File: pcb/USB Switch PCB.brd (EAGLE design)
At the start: 36 parts, among them Q1 2N7002P, Q2 2N7002P, Q3 12 MHz, X1 AMPHENOL-0001LF, X2 UE27-USBA, X3 AMPHENOL-0001LF

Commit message: Starting to look good.
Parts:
- added R10, R11: 100Ω, rcl:R0603
- added R7, R8, R9: 12kΩ, rcl:R0603
- moved EXTPWR 99.8 mm to (22.3, 2.23)
- moved R5 97.0 mm to (57.7, 9.30), turned to 0 degrees
- moved S1 96.9 mm to (26.6, 11.4)
- moved R6 96.2 mm to (57.7, 11.3), turned to 180 degrees
- moved U$4 95.8 mm to (53.9, 16.2)
- moved C9 89.6 mm to (57.7, 13.4), turned to 180 degrees
- moved C3 88.0 mm to (52.8, 12.9), turned to 270 degrees
- moved UIN 86.6 mm to (11.0, 6.97)
- moved LED2 86.3 mm to (4.93, 3.29)
- moved R2 86.3 mm to (4.93, 3.46)
- moved C4 86.3 mm to (50.7, 12.9), turned to 270 degrees
- moved X1 86.2 mm to (11.0, 1.14)
- moved R3 85.9 mm to (38.6, 13.8), turned to 90 degrees
- moved U$5 85.7 mm to (37.0, 8.66)
- moved R1 85.6 mm to (17.1, 3.33)
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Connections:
- new net GPIO15: MCU.10, R9.2
- new net GPIO2: MCU.11, R8.2
- new net N$3: MCU.14, R10.1
- new net N$5: MCU.13, R11.1
- net +5V: now also R7.1, R8.1
- net DATAGATE: now also R11.2; no longer MCU.14
- net GND: now also R9.1
- net GPIO0: now also R7.2
- net POWERGATE: now also R10.2; no longer MCU.13
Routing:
- net +5V: track 0.00 -> 127.7 mm, vias 0 -> 1
- net VCCI: track 0.00 -> 48.2 mm
- net DATAGATE: track 0.00 -> 38.9 mm
- net DATACOIL: track 0.00 -> 37.8 mm
- net +3V3: track 0.00 -> 30.0 mm, vias 0 -> 2
- net RST: track 0.00 -> 27.3 mm, vias 0 -> 1
- net GNDO: track 0.00 -> 23.3 mm
- net TXD: track 0.00 -> 21.9 mm, vias 0 -> 1
- net RXD: track 0.00 -> 17.6 mm, vias 0 -> 1
- net VCCO: track 0.00 -> 17.5 mm
- net POWERCOIL: track 0.00 -> 17.4 mm
- net POWERGATE: track 0.00 -> 15.7 mm
- net GPIO0: track 0.00 -> 13.7 mm, vias 0 -> 2
- net D-ESP: track 0.00 -> 13.5 mm
- net D+I: track 0.00 -> 13.5 mm
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- added copper zone on layer 1, net GND
- added copper zone on layer 16, net GND
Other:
- board outline added: 62.8 x 30 mm
- board text added: "EXTPWR + -"
- board text added: "USB Switch 1.1 git.erim.se/hw/usb-switch"
- board text removed: "EXT + -"
- board text removed: "USB Switch 1.1 git.erim.se /hw/usb-switch"

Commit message: Converting everything
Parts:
- removed C3: 10µF, rcl:C0603
- removed C4: 100nF, rcl:C0603
- removed D3: BAS21LT1, USB Switch PCB:SOT23
- removed R5, R6: 470Ω, rcl:R0603
- removed U$3: CH340G, ch340g:SOIC16
- removed U$4: UMH3N, USB Switch PCB:SOT363
- removed UIN: (no value), USB Switch PCB:FE05-1
- removed UOUT: (no value), USB Switch PCB:FE04-1
- removed X1, X3: AMPHENOL-0001LF, USB Switch PCB:10118192-0001LF
- added FLASH, RESET: MOMENTARY-SWITCH, USB Switch PCB:MOMENTARY-SWITCH
- added J1: (no value), SparkFun-Connectors:1X06
- added U$6: USB-B, USB Switch PCB:USB-B
- moved LED2 4.58 mm to (2.39, 7.11)
- moved R2 4.58 mm to (2.39, 7.26)
- moved LED1 4.02 mm to (18.4, 7.11)
- moved R1 4.02 mm to (18.4, 7.14)
- moved D2 2.03 mm to (7.74, 15.0)
- moved Q2 2.03 mm to (12.8, 15.0)
- moved U$2 2.03 mm to (7.87, 15.0)
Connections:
- removed net D+ESP: U$3.5, X3.D+
- removed net D-ESP: U$3.6, X3.D-
- removed net DTR: U$3.13, U$4.2, U$4.4
- removed net ID: UIN.4, X1.ID
- removed net N$4: D3.1, X3.VCC
- removed net N$7: R5.2, U$3.2
- removed net N$8: R6.2, U$3.3
- removed net RTS: U$3.14, U$4.1, U$4.5
- new net ADC: MCU.2
- net +3V3: no longer C3.1, C4.1, U$3.16
- net +5V: now also J1.4; no longer D3.3, U$3.4
- net D+I: now also U$6.3; no longer UIN.3, X1.D+
- net D+O: no longer UOUT.3
- net D-I: now also U$6.2; no longer UIN.2, X1.D-
- net D-O: no longer UOUT.2
- net GND: now also FLASH.P$3, FLASH.P$4, J1.6, RESET.P$3, RESET.P$4, U$6.4, U$6.P$1, U$6.P$2; no longer C3.2, C4.2, U$3.1, UIN.5, X1.GND, X1.P$1, X1.P$2, X1.P$3, X1.P$4, X3.GND, X3.P$1, X3.P$2, X3.P$3, X3.P$4
- net GNDO: no longer UOUT.4
- net GPIO0: now also FLASH.P$1, FLASH.P$2; no longer U$4.3
- net RST: now also RESET.P$1, RESET.P$2; no longer U$4.6
- net RXD: now also J1.3; no longer R6.1
- net TXD: now also J1.2; no longer R5.1
- net VCCI: now also U$6.1; no longer UIN.1, X1.VCC
- net VCCO: no longer UOUT.1
- net XI: no longer U$3.7
- net XO: no longer U$3.8
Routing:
- net +5V: track 127.7 -> 0.00 mm, vias 1 -> 0
- net VCCI: track 48.2 -> 0.00 mm
- net DATAGATE: track 38.9 -> 0.00 mm
- net DATACOIL: track 37.8 -> 0.00 mm
- net +3V3: track 30.0 -> 0.00 mm, vias 2 -> 0
- net RST: track 27.3 -> 0.00 mm, vias 1 -> 0
- net GNDO: track 23.3 -> 0.00 mm
- net TXD: track 21.9 -> 0.00 mm, vias 1 -> 0
- net RXD: track 17.6 -> 0.00 mm, vias 1 -> 0
- net VCCO: track 17.5 -> 0.00 mm
- net POWERCOIL: track 17.4 -> 0.00 mm
- net POWERGATE: track 15.7 -> 0.00 mm
- net GPIO0: track 13.7 -> 0.00 mm, vias 2 -> 0
- net D-ESP: track 13.5 -> 0.00 mm
- net D+I: track 13.5 -> 0.00 mm
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
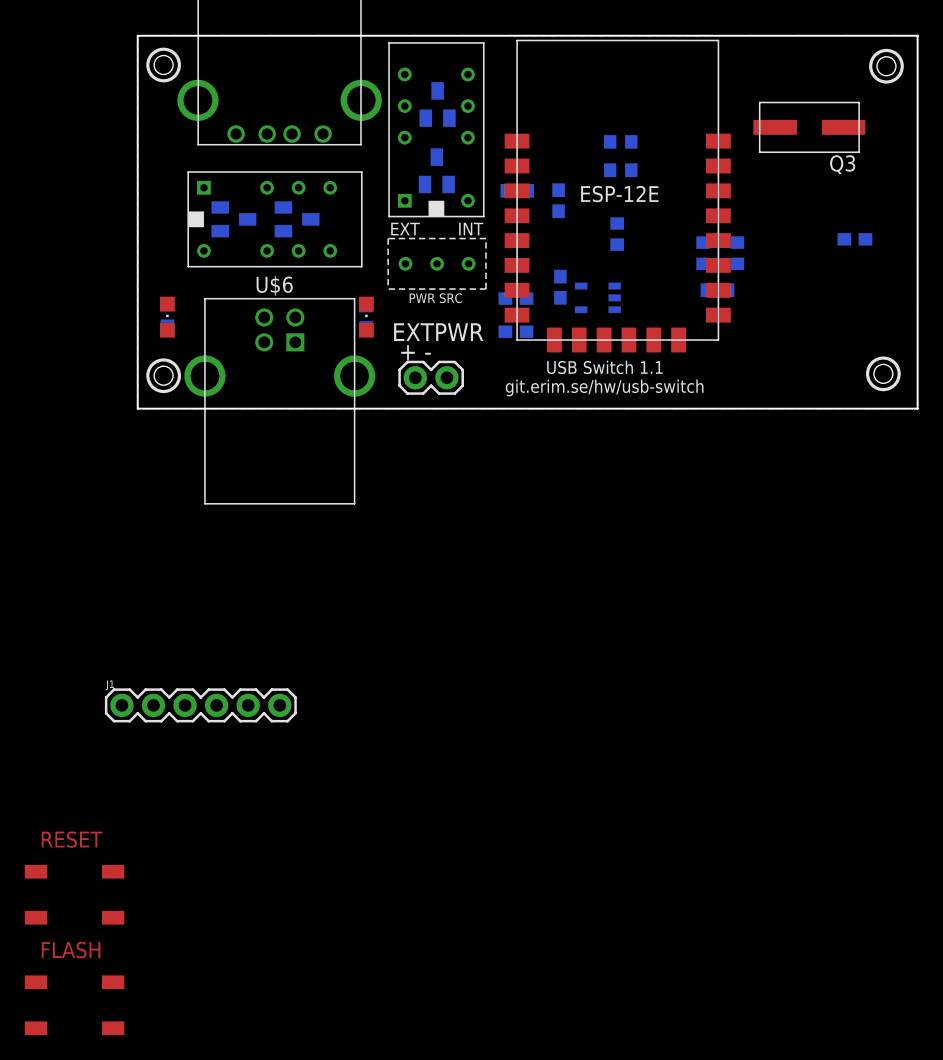
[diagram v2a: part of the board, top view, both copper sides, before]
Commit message: Aded momentary switch from banggood.
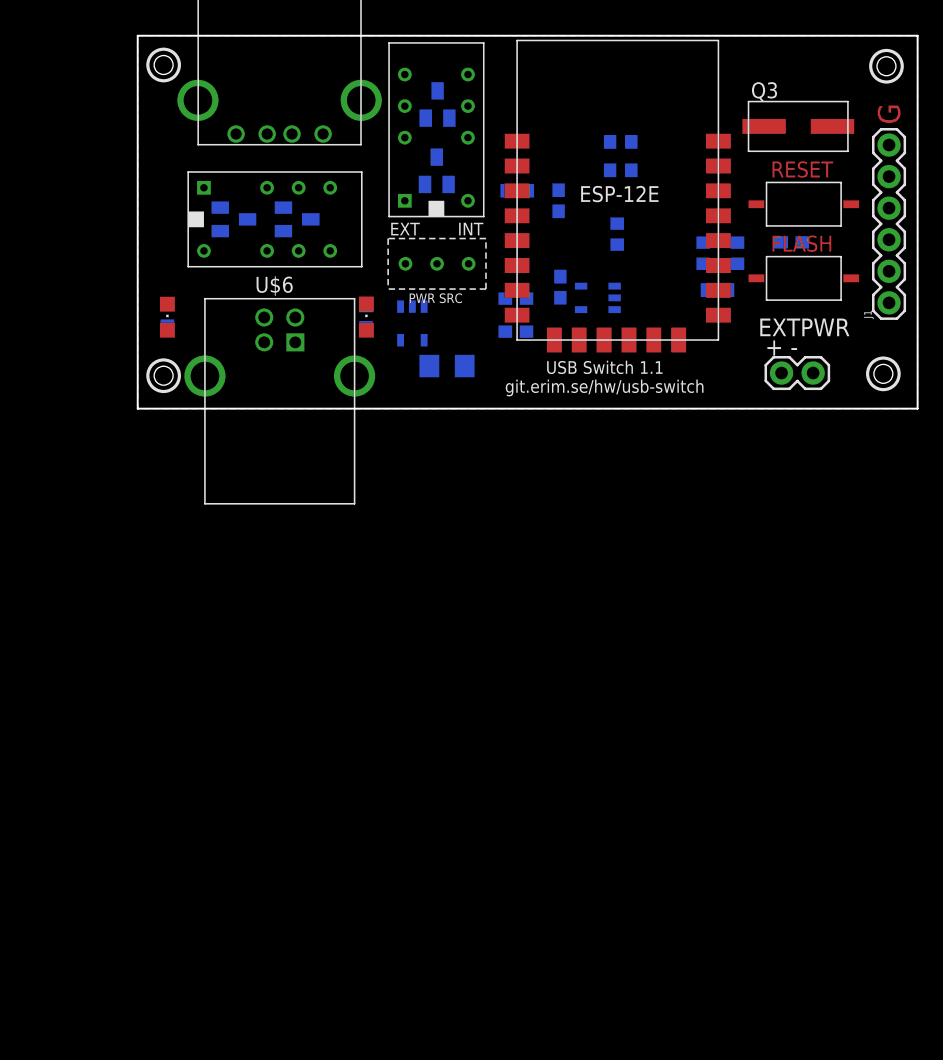
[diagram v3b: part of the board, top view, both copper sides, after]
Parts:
- added R5: 82mΩ, rcl:R1206
- added U$3: TCS888, USB Switch PCB:SOT-23-5
- moved FLASH 82.8 mm to (53.6, 10.2)
- moved RESET 80.8 mm to (53.6, 16.2)
- moved J1 69.7 mm to (60.5, 8.26), turned to 90 degrees
- moved EXTPWR 29.5 mm to (51.8, 2.61)
- moved C9 5.09 mm to (52.6, 13.1)
- moved Q3 0.90 mm to (53.1, 22.5), turned to 0 degrees
- moved C6 0.90 mm to (50.4, 22.5)
- moved C5 0.76 mm to (55.9, 22.4)
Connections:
- new net VCCU: R5.1, U$1.4, U$3.3
- net +5V: now also U$3.5
- net ADC: now also U$3.1
- net GND: now also FLASH.P$2, RESET.P$2, U$3.2; no longer FLASH.P$3, FLASH.P$4, RESET.P$3, RESET.P$4
- net GPIO0: no longer FLASH.P$2
- net RST: no longer RESET.P$2
- net VCCI: now also R5.2, U$3.4; no longer U$1.4
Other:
- board text added: "G"

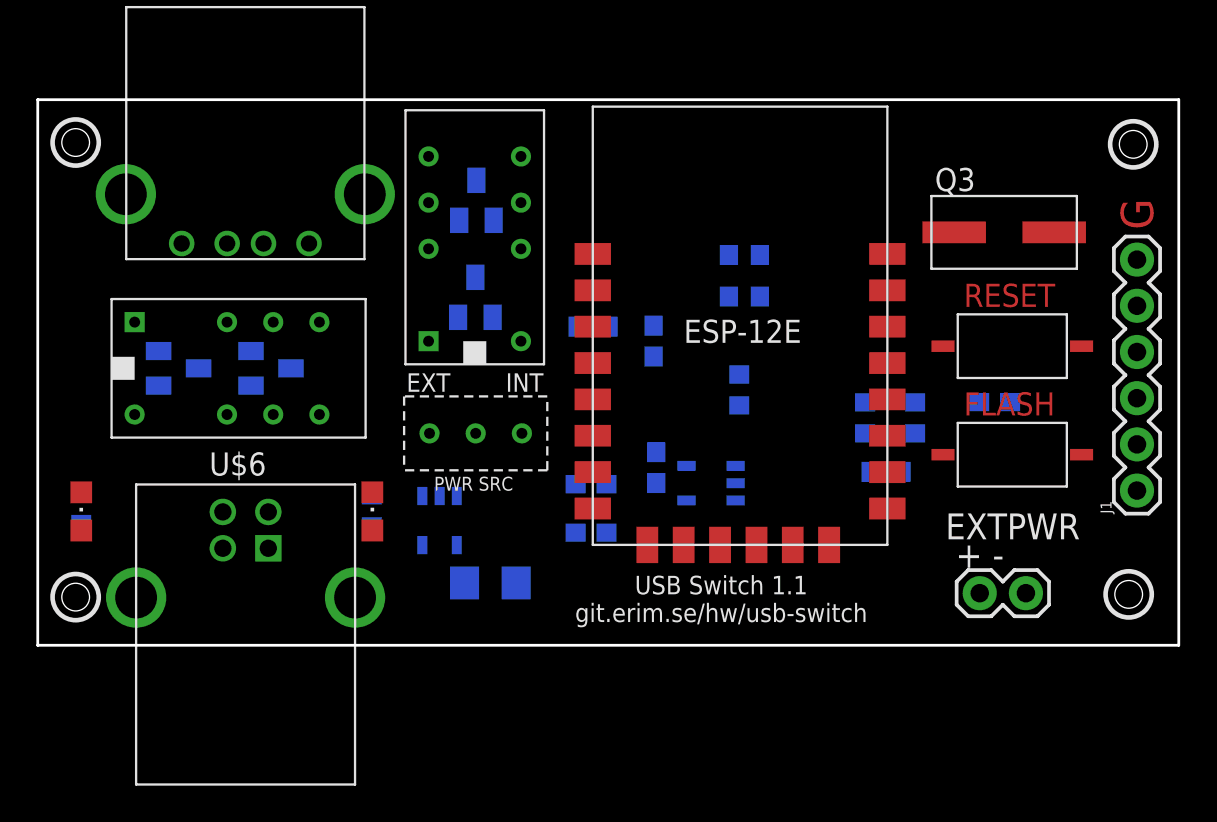
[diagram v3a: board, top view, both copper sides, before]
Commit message: Current measurement circuit now done.
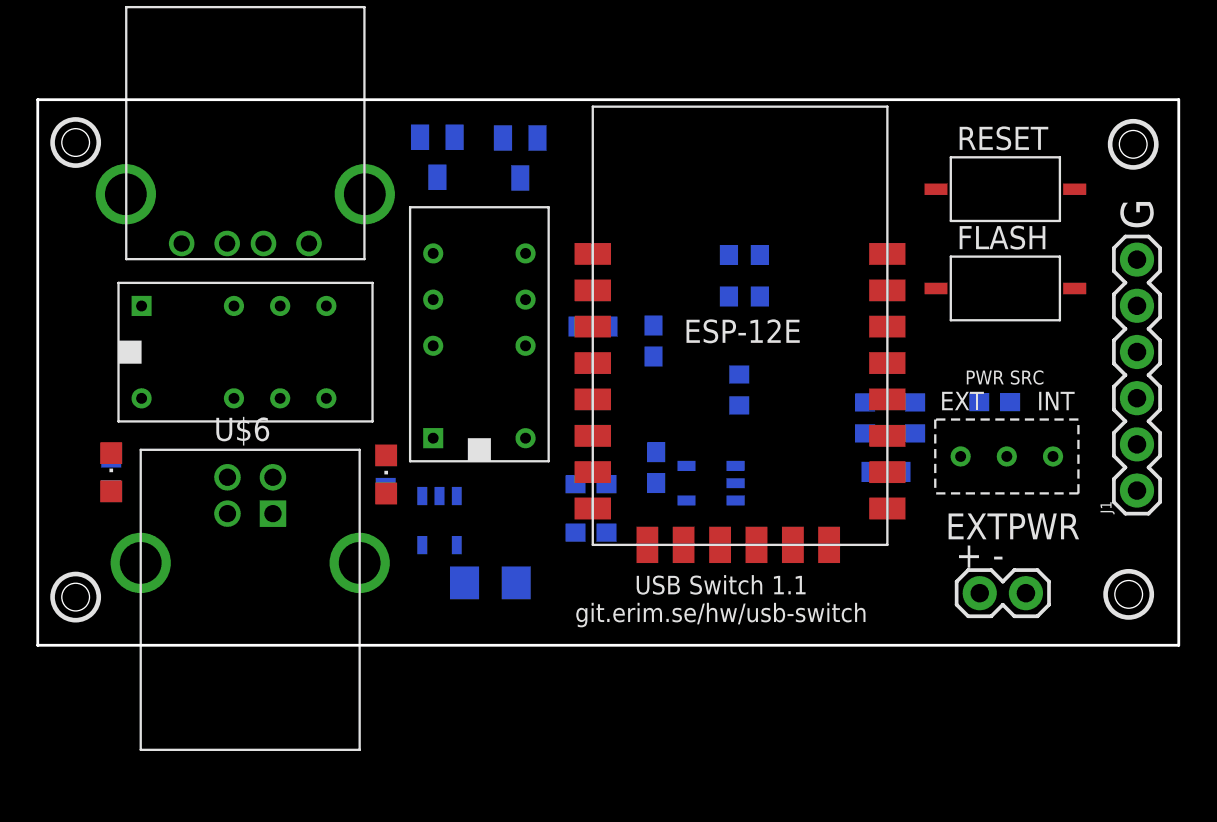
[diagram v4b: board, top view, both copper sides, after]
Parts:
- removed C5, C6: 20pF, rcl:C0603
- removed D1, D2: BAS21LT1, USB Switch PCB:SOT23
- removed Q3: 12 MHz, USB Switch PCB:CSM-3X
- moved S1 29.2 mm to (55.8, 10.1)
- moved Q2 17.9 mm to (26.5, 26.5), turned to 180 degrees
- moved FLASH 9.15 mm to (53.2, 19.4)
- moved RESET 8.64 mm to (53.2, 24.8)
- moved U$1 5.34 mm to (24.3, 13.7)
- moved Q1 3.20 mm to (22.0, 26.6), turned to 180 degrees
- moved LED2 2.72 mm to (4.04, 9.26)
- moved R2 2.52 mm to (4.04, 9.17)
- moved R1 2.29 mm to (19.1, 9.30)
- moved LED1 2.17 mm to (19.2, 9.14)
- moved U$6 1.92 mm to (11.7, 6.99)
- moved U$2 0.97 mm to (8.25, 15.9)
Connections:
- removed net XI: C6.1, Q3.P$2
- removed net XO: C5.1, Q3.P$1
- net +5V: no longer D1.3, D2.3
- net DATACOIL: no longer D2.1
- net GND: no longer C5.2, C6.2
- net POWERCOIL: no longer D1.1

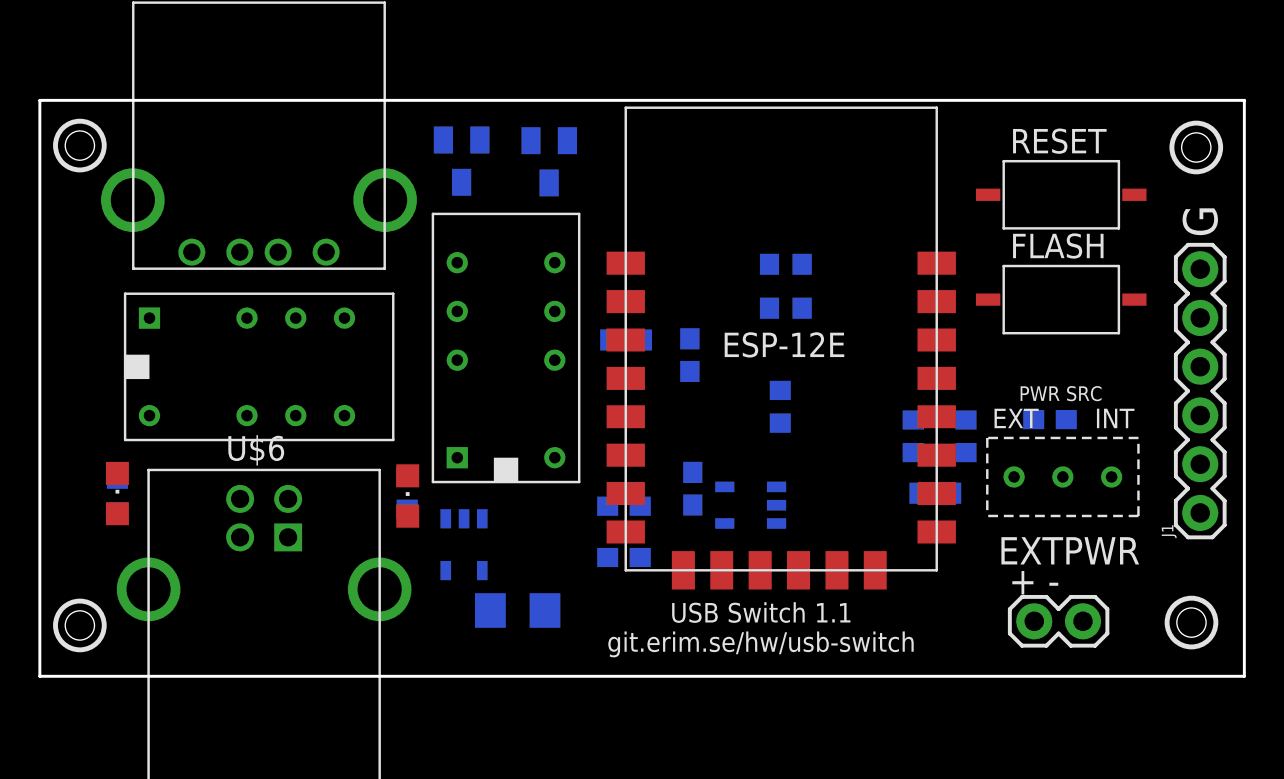
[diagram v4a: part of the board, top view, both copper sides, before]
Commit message: Remade PCB layout.
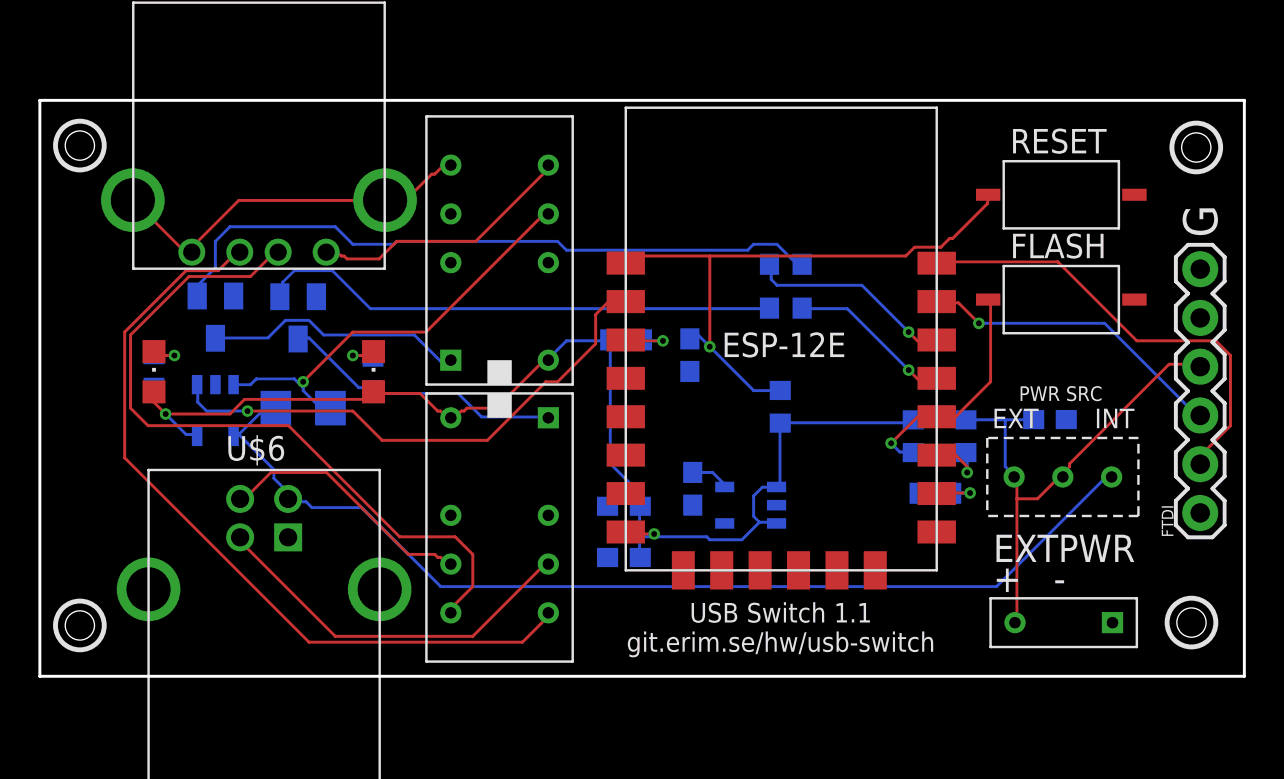
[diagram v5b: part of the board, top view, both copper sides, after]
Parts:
- removed EXTPWR: (no value), SparkFun-Connectors:1X02
- added U$4: TERMINAL-BLOCK, USB Switch PCB:TERMINAL-BLOCK
- moved U$2 16.5 mm to (23.9, 10.7), turned to 180 degrees
- moved Q2 15.4 mm to (13.5, 18.4)
- moved R5 15.4 mm to (13.7, 13.7)
- moved Q1 15.2 mm to (9.15, 18.5)
- moved U$3 14.7 mm to (9.14, 13.6)
- moved R2 6.75 mm to (5.95, 15.6)
- moved LED1 6.71 mm to (17.4, 15.6)
- moved LED2 6.63 mm to (5.95, 15.6)
- moved R1 6.47 mm to (17.4, 15.5)
- moved U$1 5.09 mm to (23.9, 18.8)
- renumbered J1 to FTDI
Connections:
- net +5V: now also U$4.P; no longer EXTPWR.1
- net GND: now also U$4.N; no longer EXTPWR.2
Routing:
- net +5V: track 0.00 -> 94.4 mm, vias 0 -> 2
- net VCCI: track 0.00 -> 54.8 mm
- net D+O: track 0.00 -> 41.2 mm
- net D-O: track 0.00 -> 37.9 mm
- net POWERGATE: track 0.00 -> 35.3 mm
- net RST: track 0.00 -> 31.3 mm, vias 0 -> 1
- net ADC: track 0.00 -> 28.0 mm, vias 0 -> 1
- net DATAGATE: track 0.00 -> 27.3 mm
- net TXD: track 0.00 -> 23.7 mm
- net VCCU: track 0.00 -> 22.5 mm, vias 0 -> 1
- net D+I: track 0.00 -> 19.9 mm
- net GNDO: track 0.00 -> 19.7 mm
- net RXD: track 0.00 -> 16.2 mm, vias 0 -> 1
- net DATACOIL: track 0.00 -> 14.8 mm
- net VCCO: track 0.00 -> 13.9 mm
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
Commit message: Is this final? It sure feels like final!
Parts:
- removed U$6: USB-B, USB Switch PCB:USB-B
- added DISP: (no value), SparkFun-Connectors:1X04
- added USBIN: USB-B, USB Switch PCB:USB-B
- moved LED1 3.69 mm to (13.7, 15.7)
- moved LED2 3.18 mm to (9.12, 15.7)
- moved Q2 0.25 mm to (13.7, 18.4)
- renumbered U$1 to PWR, U$2 to DAT, U$3 to MEAS, U$4 to EXTPWR, U$5 to REG, X2 to USBOUT
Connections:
- new net SCK: DISP.3, MCU.14
- new net SDA: DISP.4, MCU.13
- net +5V: now also DISP.2; no longer S1.S
- net D+I: now also USBIN.3; no longer U$6.3
- net D-I: now also USBIN.2; no longer U$6.2
- net GND: now also DISP.1, MCU.15, USBIN.4, USBIN.P$1, USBIN.P$2; no longer MCU.9, U$6.4, U$6.P$1, U$6.P$2
- net GPIO0: now also MCU.18; no longer MCU.12
- net GPIO15: now also MCU.16; no longer MCU.10
- net GPIO2: now also MCU.17; no longer MCU.11
- net N$3: now also MCU.20; no longer MCU.14
- net N$5: now also MCU.19; no longer MCU.13
- net RXD: now also MCU.21; no longer MCU.15
- net TXD: now also MCU.22; no longer MCU.16
- net VCCI: now also USBIN.1; no longer U$6.1
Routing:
- net SCK: track 0.00 -> 61.2 mm
- net SDA: track 0.00 -> 55.4 mm
- net +5V: track 94.4 -> 109.6 mm, vias 2 -> 0
- net DATAGATE: track 27.3 -> 39.7 mm
- net D-O: track 37.9 -> 28.0 mm, vias 0 -> 1
- net D+O: track 41.2 -> 32.4 mm, vias 0 -> 1
- net POWERGATE: track 35.3 -> 43.2 mm
- net RST: track 31.3 -> 27.4 mm, vias 1 -> 2
- net ADC: track 28.0 -> 31.8 mm
- net N$1: track 2.35 -> 3.82 mm
- net TXD: track 23.7 -> 22.3 mm
- net N$2: track 2.20 -> 3.31 mm
- net RXD: track 16.2 -> 17.1 mm, vias 1 -> 0
- net D+I: track 19.9 -> 20.5 mm
